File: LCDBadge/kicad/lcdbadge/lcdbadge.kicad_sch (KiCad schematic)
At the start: 19 parts, among them SW1 SW_Push, SW2 SW_Push, SW3 SW_Push, SW4 SW_Push, X1 Badgelife_sao_connector_v169b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

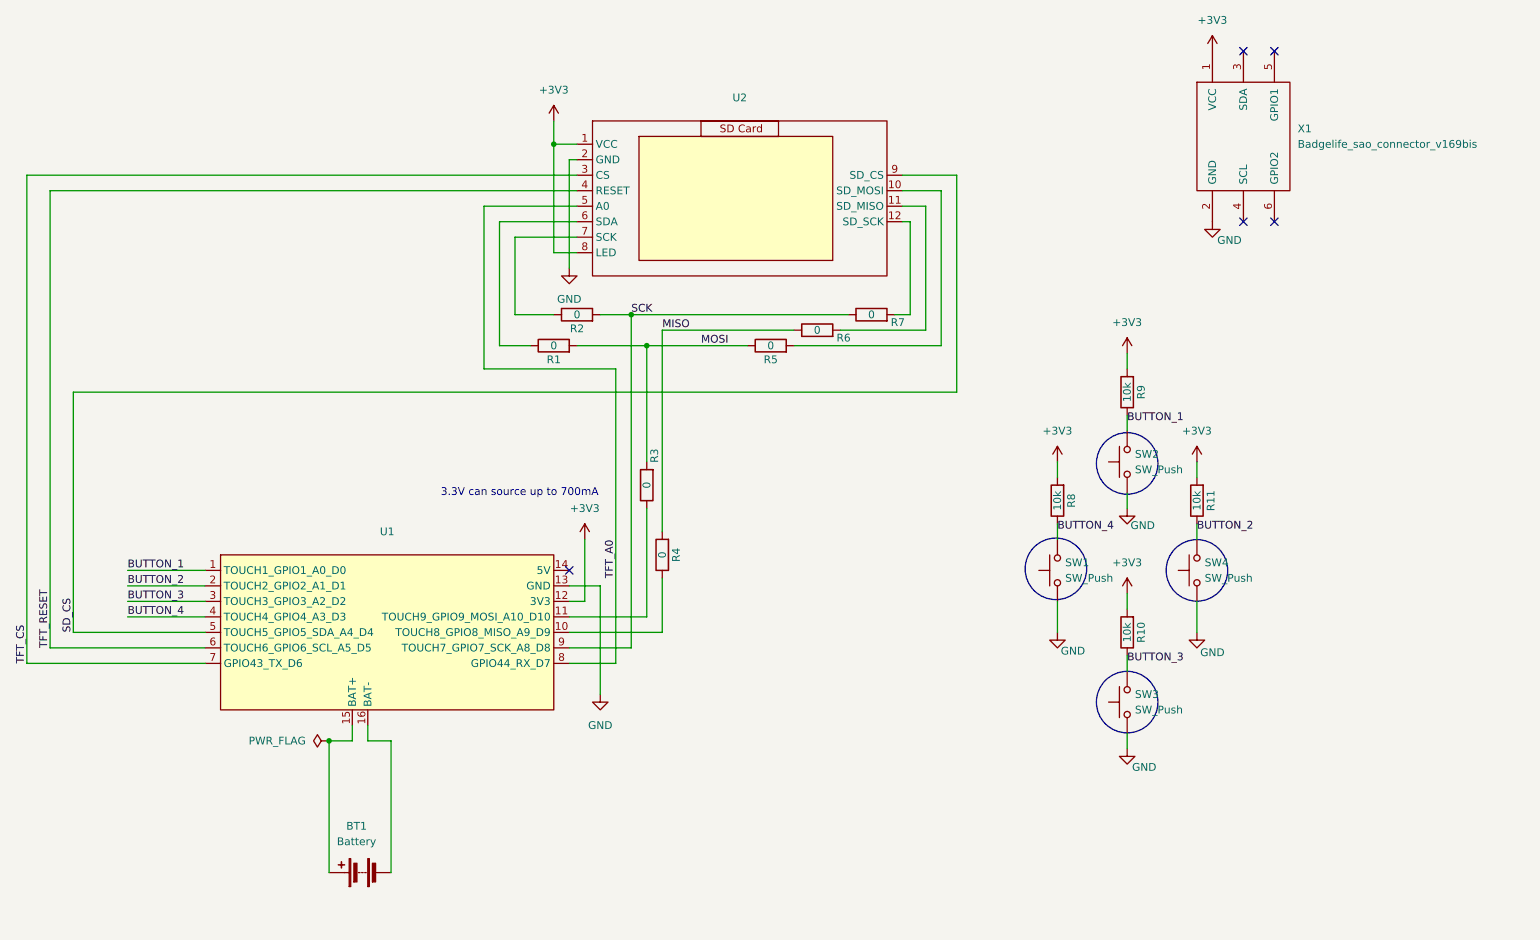
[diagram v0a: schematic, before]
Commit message: routed board updated button changed from route to large vias for module
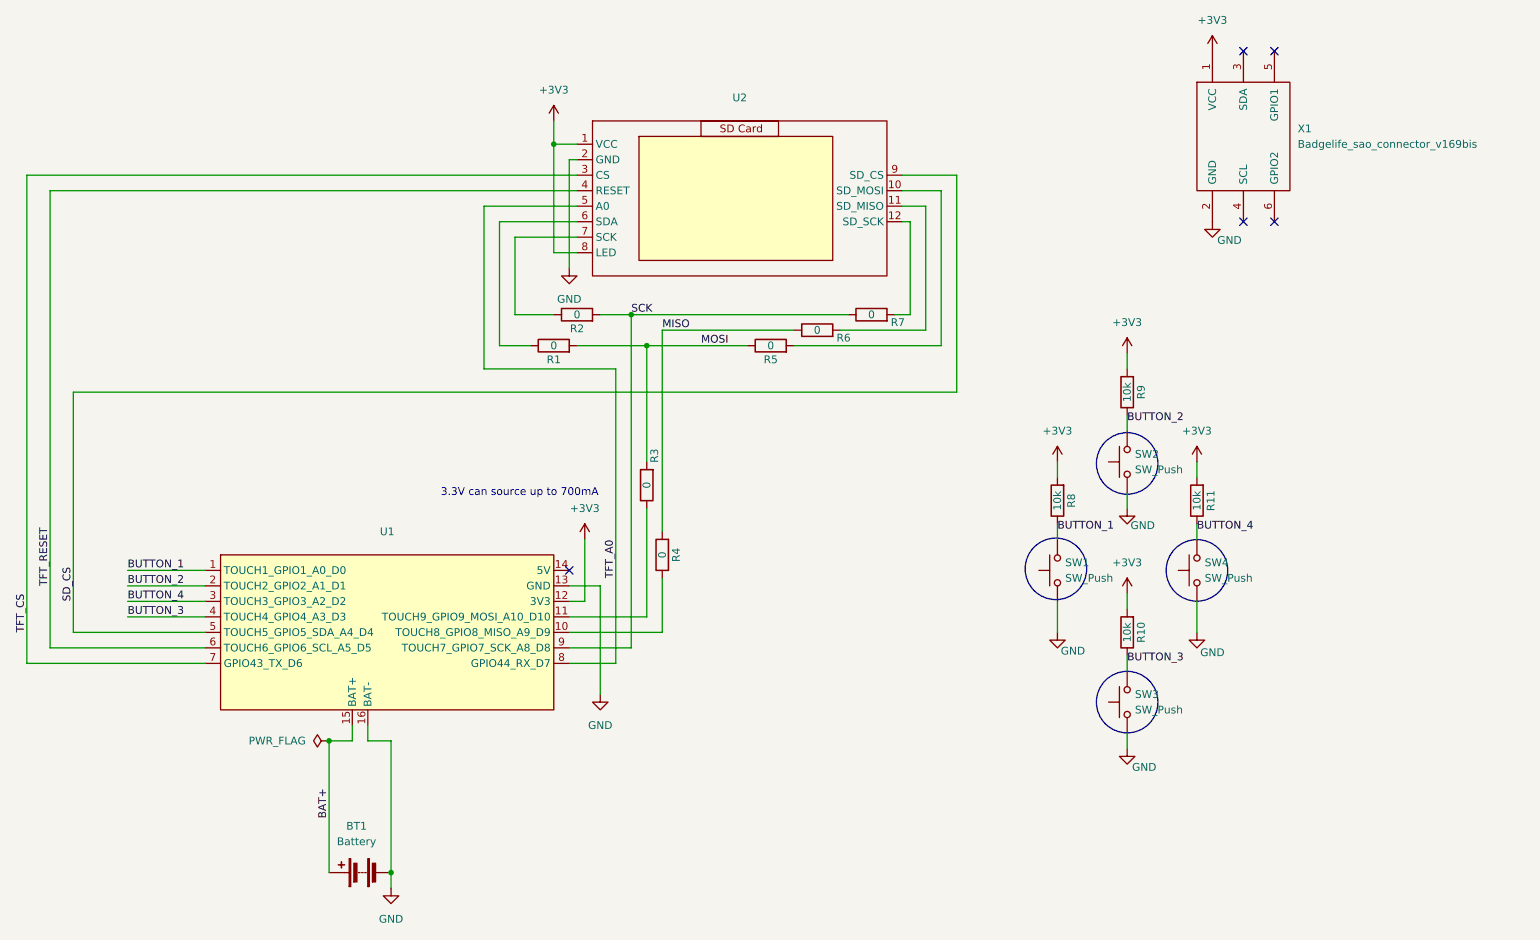
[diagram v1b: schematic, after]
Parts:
- SW1, SW2, SW3, SW4: footprint Button_Switch_THT:SW_Tactile_Straight_KSA0Axx1LFTR -> Button_Switch_THT:SW_PUSH_6mm_H4.3mm
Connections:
- net BUTTON_1: now also R8.1, SW1.2; no longer R9.1, SW2.2
- net BUTTON_2: now also R9.1, SW2.2; no longer R11.1, SW4.2
- net BUTTON_3: now also U1.4 (TOUCH4_GPIO4_A3_D3); no longer U1.3 (TOUCH3_GPIO3_A2_D2)
- net BUTTON_4: now also R11.1, SW4.2, U1.3 (TOUCH3_GPIO3_A2_D2); no longer R8.1, SW1.2, U1.4 (TOUCH4_GPIO4_A3_D3)
- net GND: now also BT1.2 (-), U1.16 (BAT-)
- net BAT+: now reaches BT1.1 (+), U1.15 (BAT+)

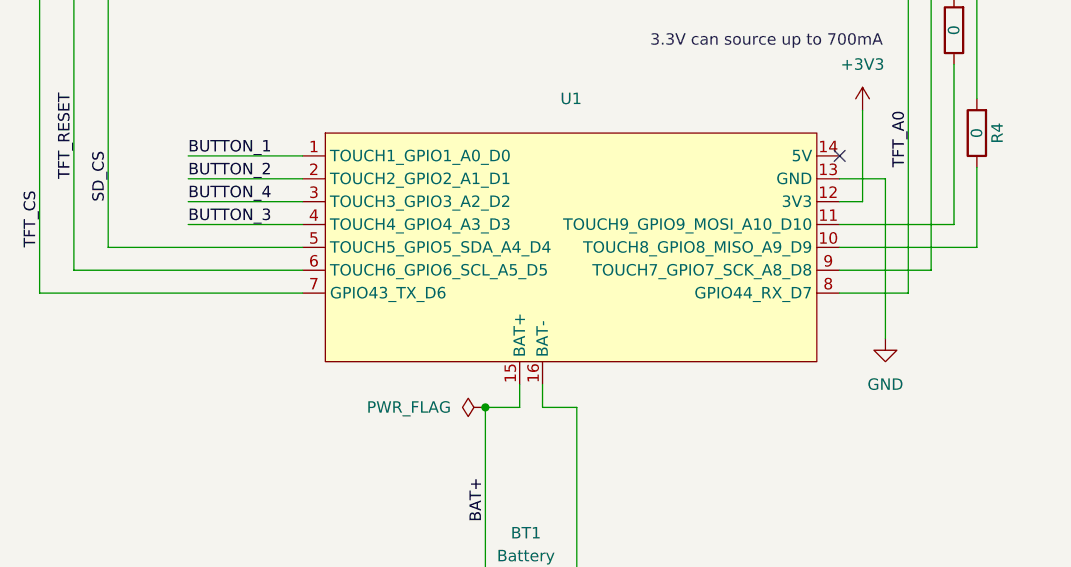
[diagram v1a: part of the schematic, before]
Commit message: rotated esp moved resistors away from sd card holder
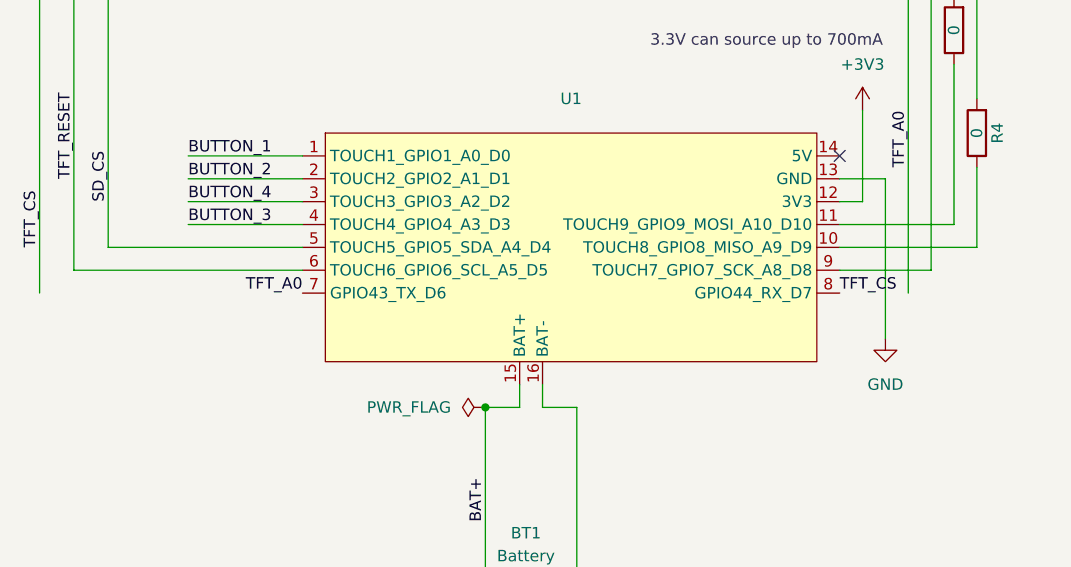
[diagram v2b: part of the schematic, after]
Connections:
- net TFT_A0: now also U1.7 (GPIO43_TX_D6); no longer U1.8 (GPIO44_RX_D7)
- net TFT_CS: now also U1.8 (GPIO44_RX_D7); no longer U1.7 (GPIO43_TX_D6)
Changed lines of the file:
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@@
-	(wire
-		(pts
-			(xy 120.65 130.81) (xy 128.27 130.81)
-		)
-		(stroke
-			(width 0)
-			(type default)
-		)
-	)
 	(wire
 		(pts
@@
 		(pts
 			(xy 212.09 119.38) (xy 212.09 121.92)
-		)
-		(stroke
-			(width 0)
-			(type default)
-		)
-	)
-	(wire
-		(pts
-			(xy 60.96 130.81) (xy 31.75 130.81)
 		)
 		(stroke
@@
 		)
 	)
+	(label "TFT_CS"
+		(at 120.65 130.81 0)
+		(fields_autoplaced yes)
+		(effects
+			(font
+				(size 1.27 1.27)
+			)
+			(justify left bottom)
+		)
+	)
 	(label "MOSI"
 		(at 142.24 78.74 0)
@@
 		)
 	)
+	(label "TFT_A0"
+		(at 60.96 130.81 180)
+		(fields_autoplaced yes)
+		(effects
+			(font
+				(size 1.27 1.27)
+			)
+			(justify right bottom)
+		)
+	)
